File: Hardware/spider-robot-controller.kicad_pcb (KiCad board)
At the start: 2 copper layers, 25 parts, among them P1 SERVO_HEADER, P10 SERVO_HEADER, P11 SERVO_HEADER, P12 SERVO_HEADER, P13 Bluetooth_header, P2 SERVO_HEADER, P24 CONN_01X01, P25 CONN_01X01, P3 SERVO_HEADER, P4 SERVO_HEADER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

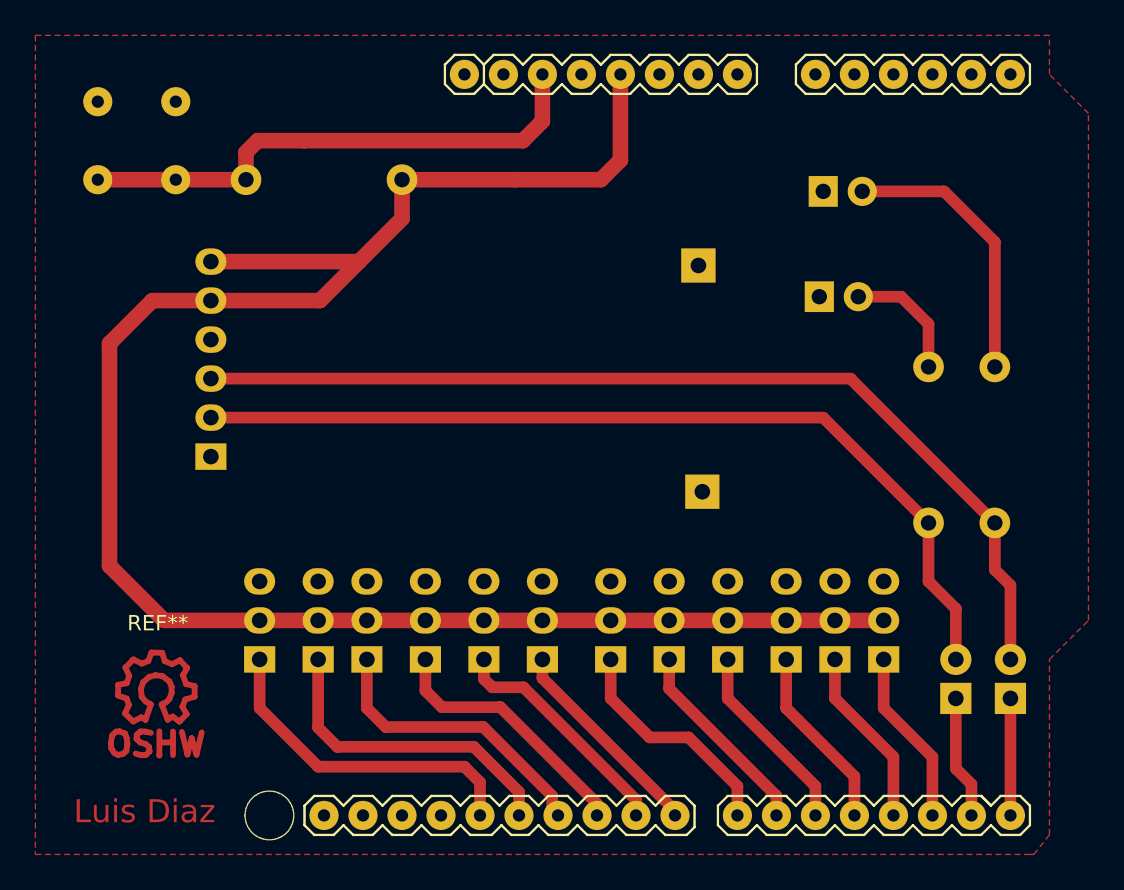
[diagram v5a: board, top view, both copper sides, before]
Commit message: Improved layout of the board - BT module fits better
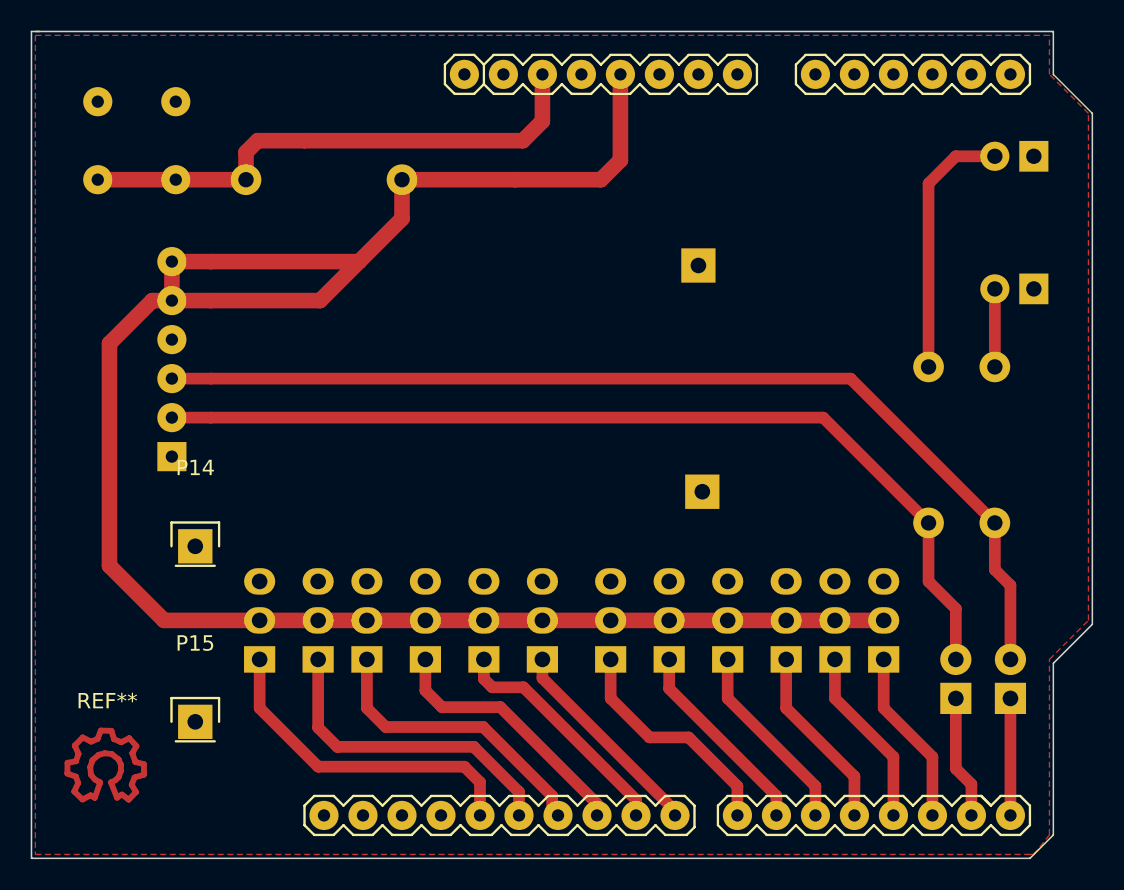
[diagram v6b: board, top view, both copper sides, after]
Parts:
- added P14: CONN_01X01, Pin_Headers:Pin_Header_Straight_1x01, F.Cu at (188.2, 82.8)
- added P15: CONN_01X01, Pin_Headers:Pin_Header_Straight_1x01, F.Cu at (188.2, 94.2)
- moved D2 16.7 mm to (242.8, 57.4), turned to 180 degrees
- moved D1 15.1 mm to (242.8, 66.0), turned to 180 degrees
- moved REF** 6.06 mm to (182.4, 97.3)
- moved P13 2.54 mm to (186.7, 77.0)
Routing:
- net Net-(D1-Pad2): track 18.1 -> 5.08 mm
- net Net-(D2-Pad2): track 8.10 -> 17.0 mm
- net VCC: track 121.3 -> 126.4 mm
- net BTX: track 64.3 -> 66.8 mm
- net BRX: track 59.2 -> 61.7 mm
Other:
- board outline added: 69.1 x 53.8 mm
- board text removed: "Luis Diaz"
